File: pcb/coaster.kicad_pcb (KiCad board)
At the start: 2 copper layers, 50 x 50 mm, 21 parts, among them J1 UPDI, Q1 2N7002, SW1 TS-1187A-B-A-B, U1 ATtiny402-SSN

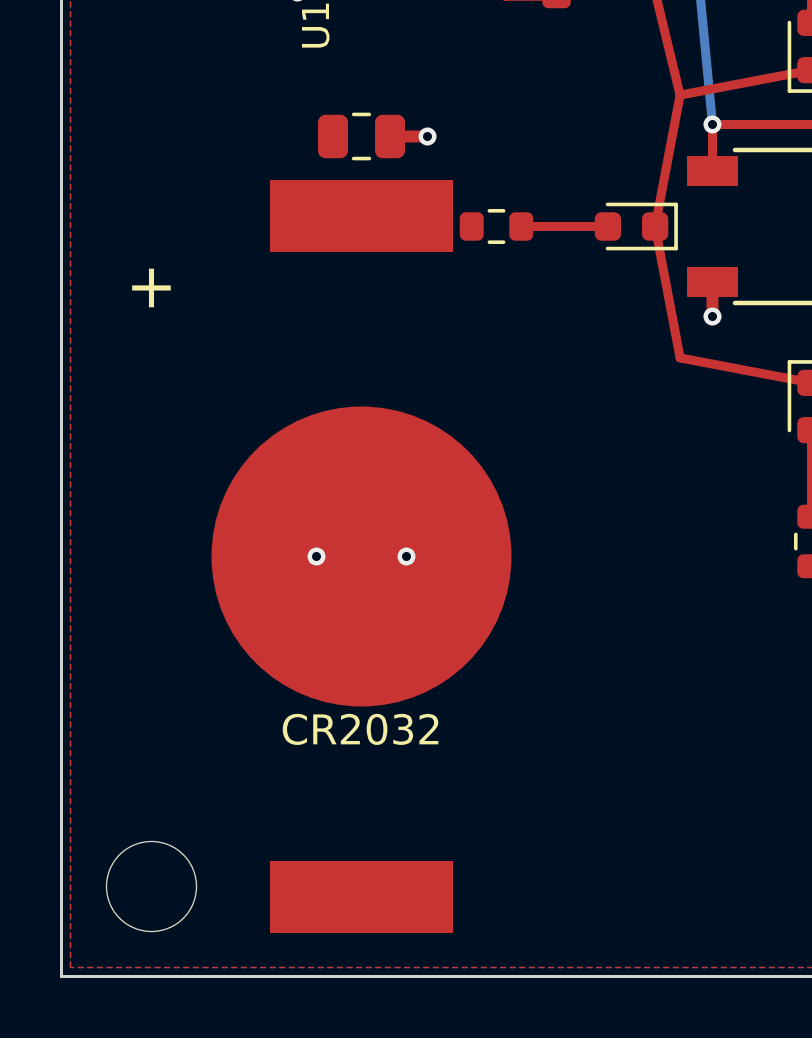
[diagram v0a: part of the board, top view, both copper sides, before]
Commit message: Switch battery to CR2016 (MY-2016-02) to slim the enclosure
The battery holder was the tallest component, sitting just above the
button. Swap the CR2032 holder (MY-2032-12, 3.6mm tall) for a CR2016
holder (MY-2016-02, 2.2mm) -- 1.4mm lower. ~75mAh still gives 2+ years
at a few presses a day, since µA sleep dominates and presses are ~free.

New footprint land pattern is from the MY-2016-02 datasheet (WD-CP-0081):
clip pads 5.6x1.75mm at 21.75mm center-to-center, 10mm center contact --
distinct from the 2032's pattern, verified against both datasheets.

The board file also re-baselines to generate.py's deterministic seeded
UUID layout; the file committed in 8bfbe22 still carried the pre-seed
ordering, so this is the first regeneration that matches the seed.
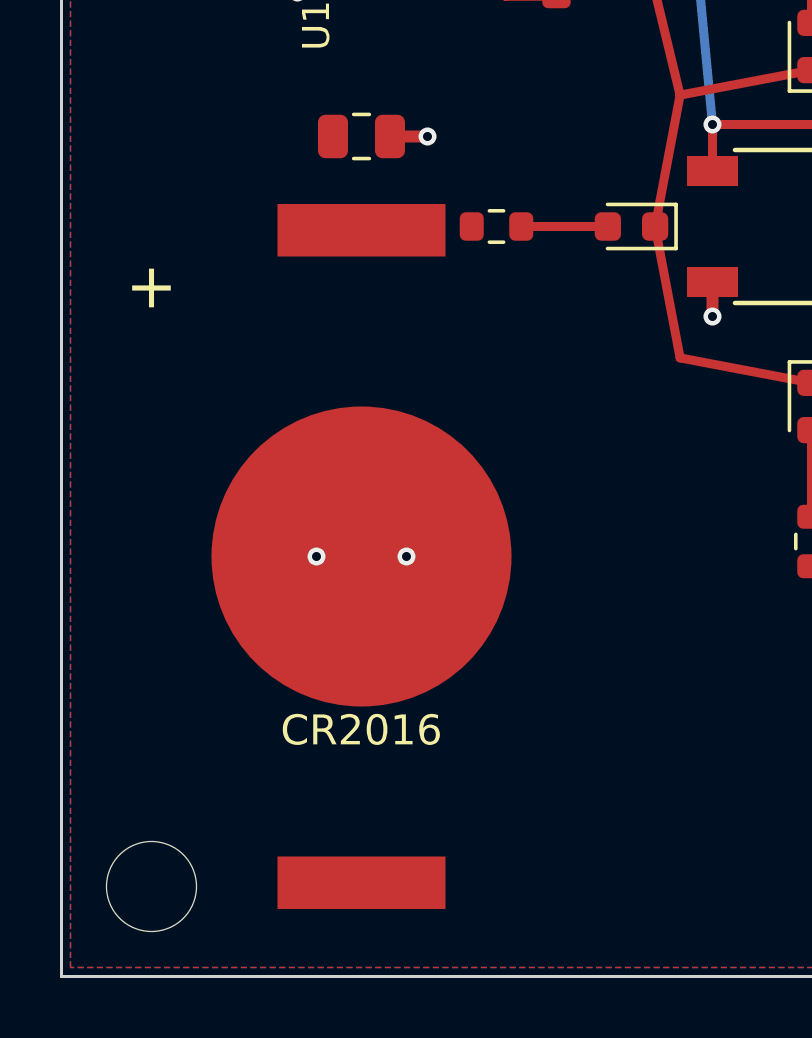
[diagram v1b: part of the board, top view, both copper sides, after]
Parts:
- BT1: value CR2032 -> CR2016; footprint MY-2032-12 -> MY-2016-02

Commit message: Swap Q1 to AO3400A for logic-level gate drive
The 2N7002's gate threshold is spec'd up to 2.5V worst-case, which a
CR2016 spends most of its life barely above -- a high-threshold part
plus a worn cell reads as dim or flickering LEDs. The AO3400A (LCSC
C20917, JLCPCB basic catalog, same SOT-23 pinout and price) is fully
enhanced at 2.5V with Vgs(th) of 0.65-1.45V.
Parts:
- Q1: value 2N7002 -> AO3400A
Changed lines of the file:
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@@
 			)
 		)
-		(property "Value" "2N7002"
+		(property "Value" "AO3400A"
 			(at 0 2.4 90)
 			(layer "F.Fab")

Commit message: Move battery-return vias out of the cell contact pad
The CR2016 presses directly on BT1 pad 2 (bare copper, mask-defined),
and the two GND stitching vias sat inside that 10mm contact circle --
drill dimples and flux right at the contact surface risk an
intermittent battery connection that presents as random resets. The
vias now sit just outside the circle, fed by short spokes from the pad
center.
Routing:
- net GND: track 9.52 -> 21.9 mm
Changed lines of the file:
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@@
+	)
+	(segment
+		(start 10 36)
+		(end 16.2 36)
+		(width 0.4)
+		(layer "F.Cu")
+		(net "GND")
 	)
 	(segment
@@
 		(start 17.45 12.9375)
 		(end 18.5 12.94)
+		(width 0.4)
+		(layer "F.Cu")
+		(net "GND")
+	)
+	(segment
+		(start 10 36)
+		(end 3.8 36)
 		(width 0.4)
 		(layer "F.Cu")
@@
 	)
 	(via
-		(at 11.5 36)
+		(at 3.8 36)
 		(size 0.6)
 		(drill 0.3)
@@
 	)
 	(via
-		(at 8.5 36)
+		(at 16.2 36)
 		(size 0.6)
 		(drill 0.3)

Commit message: Upgrade LEDs to XL-1608UWC-04 for ~3x brightness at the same current
Same 0603 footprint and 120 degree viewing angle as the KT-0603W, but
400 min / 630 typ mcd at 20mA versus 173-207. Cool white, Vf 2.6-2.8V
typical, LCSC C965808 (JLCPCB extended: one more $3 feeder fee, or
$0.10/board at qty 30). Also note white soldermask in the ordering
plan -- the board face is the reflector behind the LEDs under the
clear shield.
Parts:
- L1, L2, L3, L4: value KT-0603W -> XL-1608UWC-04
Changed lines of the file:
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@@
 			)
 		)
-		(property "Value" "KT-0603W"
+		(property "Value" "XL-1608UWC-04"
 			(at 0 1.43 0)
 			(layer "F.Fab")
@@
 			)
 		)
-		(property "Value" "KT-0603W"
+		(property "Value" "XL-1608UWC-04"
 			(at 0 1.43 270)
 			(layer "F.Fab")
@@
 			)
 		)
-		(property "Value" "KT-0603W"
+		(property "Value" "XL-1608UWC-04"
 			(at 0 1.43 180)
 			(layer "F.Fab")
@@
 			)
 		)
-		(property "Value" "KT-0603W"
+		(property "Value" "XL-1608UWC-04"
 			(at 0 1.43 90)
 			(layer "F.Fab")

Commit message: Swap U1 to the ATtiny202 to cut the dominant BOM cost
Same SOIC-8 pinout, peripherals, sleep current, and firmware as the
ATtiny402 -- only flash/SRAM shrink (2KB/128B, still 7x the current
firmware) -- for $0.43 vs $0.65 (LCSC C2052951). The 402 stays a
drop-in substitute at order time: a binary built for the 202 runs on
it unmodified.
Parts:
- U1: value ATtiny402-SSN -> ATtiny202-SSN
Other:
- board text added: "U1 ATTINY202 Q1 LED DRIVER"
- board text removed: "U1 ATTINY402 Q1 LED DRIVER"
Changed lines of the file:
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@@
 			)
 		)
-		(property "Value" "ATtiny402-SSN"
+		(property "Value" "ATtiny202-SSN"
 			(at 0 3.4 270)
 			(layer "F.Fab")
@@
 		)
 	)
-	(gr_text "U1 ATTINY402   Q1 LED DRIVER"
+	(gr_text "U1 ATTINY202   Q1 LED DRIVER"
 		(at 40.4 29 90)
 		(layer "F.SilkS")

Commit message: Model the battery holder's true body and re-place it with real clearances
The MY-2016-02 footprint encoded only its copper: two clip pads and
the contact circle. The physical part is a 22.8x15.2mm chamfered frame
2.2mm tall, and the bare CR2016 overhangs it on both depth sides --
none of which was drawn on any layer, in the courtyard, or in a 3D
model, so DRC and the STEP fit-check were blind to it. Verified the
pad geometry against datasheet WD-CP-0081 (exact match, and ~1mm
tighter than the proven v0.2 CR2032 holder), then:

- Footprint: true frame + feet + cell outline on F.Fab, courtyard as
  the real envelope polygon, insertion mouth marked, and a generated
  STEP body (frame + cell) so CAD interference checks see the part.
- Placement: BT1 moves (10,36) -> (13,37.8). At the old spot the cell
  rim was tangent to the board edge and an M3 head at mounting hole H2
  would graze the frame corner; the new spot gives the cell 3mm of
  edge margin, H2 hardware ~0.7mm of frame clearance (now also policed
  by the courtyard), and keeps the south clip pad clear of R4. Mouth
  faces the west board edge so the cell slides over bare board; CPL
  orientation check noted in the ordering plan.

Battery-return vias now derive from the pad center instead of
hardcoded coordinates. DRC clean with the new courtyard active.
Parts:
- moved BT1 3.50 mm to (13.0, 37.8)
